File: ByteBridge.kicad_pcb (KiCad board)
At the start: 2 copper layers, 26 x 38 mm, 24 parts, among them J1 USB_C_Receptacle_USB2.0_16P, J2 Conn_01x04_Pin, J5 Conn_01x03_Pin, U1 AMS1117-3.3, U2 CP2102N-Axx-xQFN28

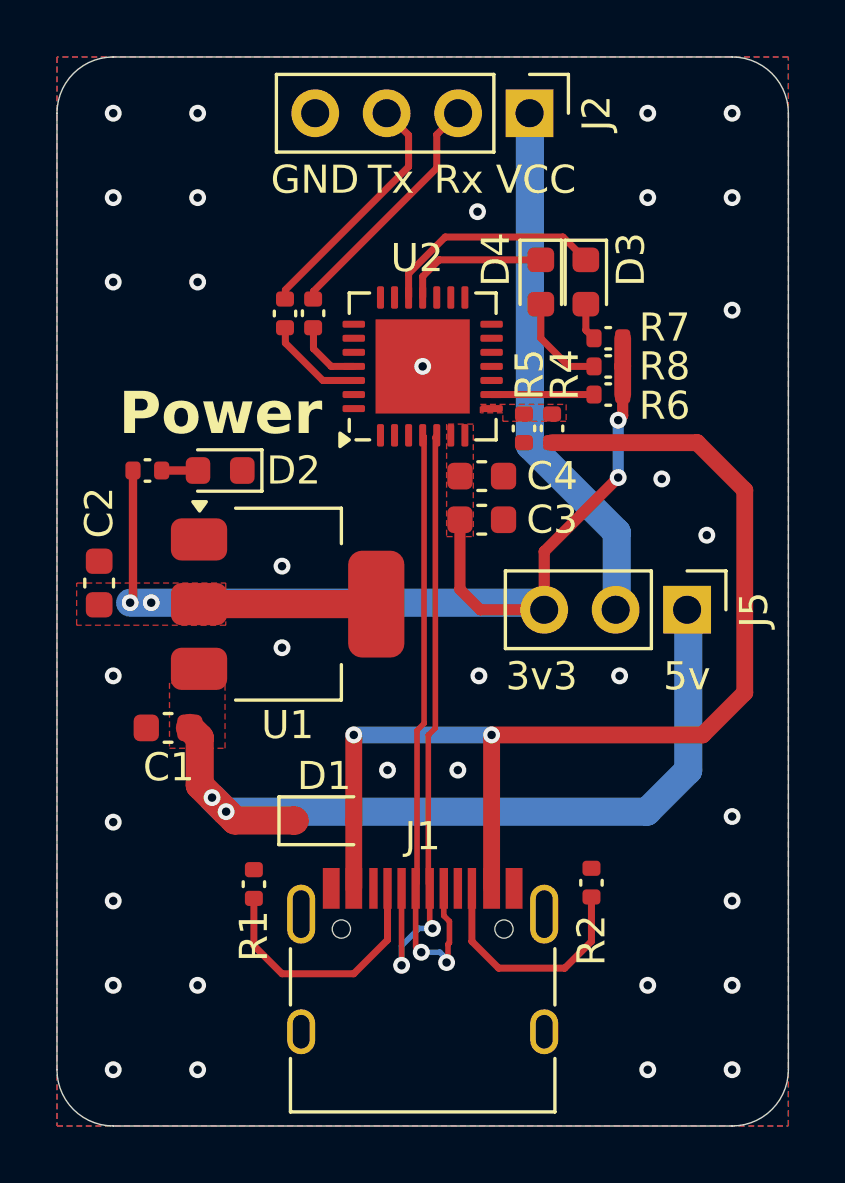
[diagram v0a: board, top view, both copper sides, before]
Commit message: feat: refactor board edge and component placement
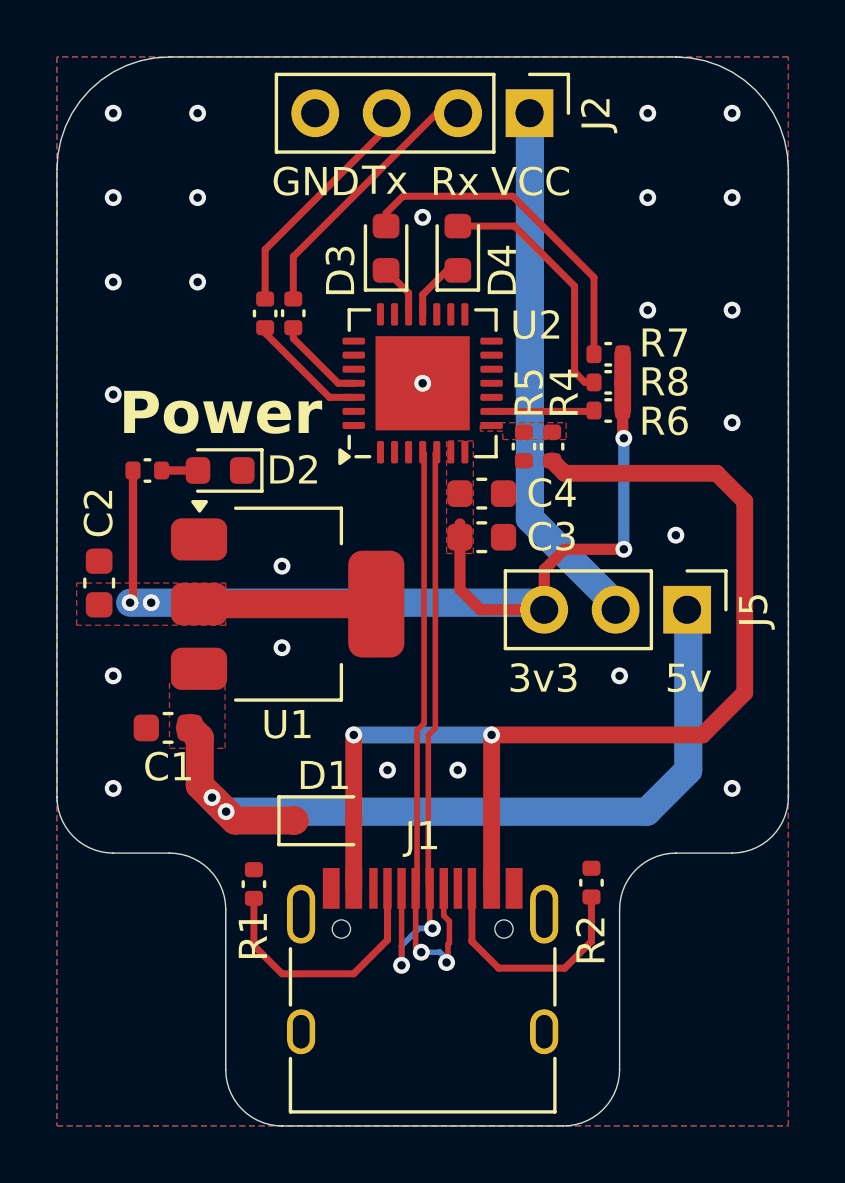
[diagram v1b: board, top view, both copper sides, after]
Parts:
- moved D3 7.20 mm to (145.6, 77.8), turned to 90 degrees
- moved D4 3.18 mm to (148.2, 77.8), turned to 90 degrees
- moved R10 0.71 mm to (142.3, 80.1)
- moved R9 0.71 mm to (141.3, 80.1)
- moved R4 0.65 mm to (151.5, 84.8)
- moved R5 0.65 mm to (150.5, 84.8)
- moved C4 0.62 mm to (149.0, 86.5)
- moved C3 0.62 mm to (149.0, 88.0)
- moved U2 0.60 mm to (146.9, 82.6)
- moved R6 0.57 mm to (153.5, 83.5)
- moved R7 0.57 mm to (153.5, 81.5)
- moved R8 0.57 mm to (153.5, 82.5)
- moved REF** 0.52 mm to (147.1, 81.5)
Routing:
- net Net-(D3-A): track 1.33 -> 12.0 mm
- net Net-(D3-K): track 8.03 -> 1.89 mm
- net Net-(D4-A): track 3.52 -> 8.93 mm
- net Net-(D4-K): track 5.19 -> 2.31 mm
- net Net-(U2-TXD): track 3.53 -> 4.29 mm
- net Net-(U2-RXD): track 2.44 -> 3.19 mm
- net /RX: track 8.74 -> 9.48 mm
- net +3.3V: track 42.9 -> 43.6 mm
- net /D-: track 22.3 -> 21.7 mm
- net /D+: track 22.3 -> 21.7 mm
- net VBUS: track 40.2 -> 39.7 mm
- net GND: vias 34 -> 25
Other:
- outline, holes or cut-outs redrawn
